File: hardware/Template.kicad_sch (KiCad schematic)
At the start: 0 parts

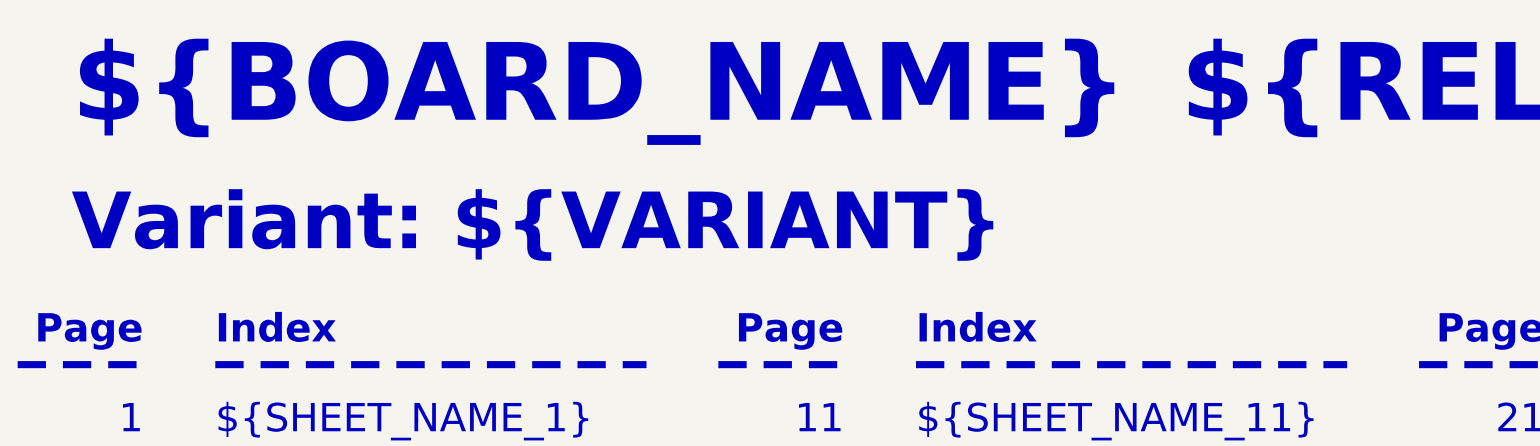
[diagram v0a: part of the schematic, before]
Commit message: Rename VARIANT variable to PCB_VARIANT
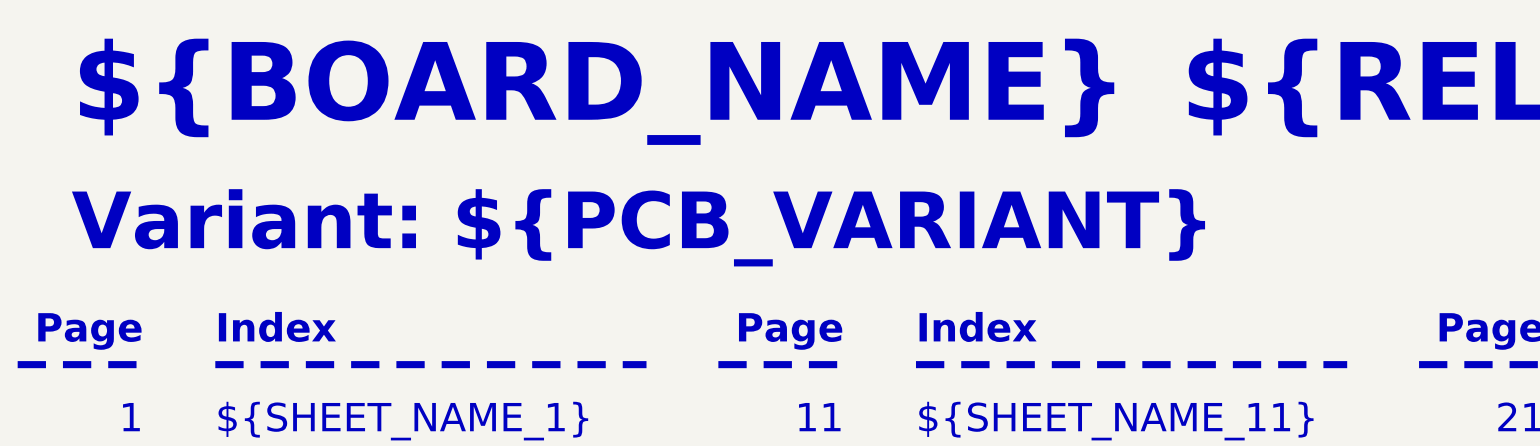
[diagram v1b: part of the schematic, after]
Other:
- note added: "Variant: ${PCB_VARIANT}"
- note removed: "Variant: ${VARIANT}"
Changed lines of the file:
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@@
 		(company "${COMPANY}")
 	)
-	(text "Variant: ${VARIANT}"
+	(text "Variant: ${PCB_VARIANT}"
 		(exclude_from_sim no)
 		(at 31.75 59.69 0)
